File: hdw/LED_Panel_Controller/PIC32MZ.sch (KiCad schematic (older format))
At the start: 3 parts

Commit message: more schematic development
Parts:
- removed U?: PIC32MZ2048EFG100-250_IPF, Housings_QFP:TQFP-100_14x14mm_Pitch0.5mm, symbol Custom_Library:PIC32MZ2048EFG100_IPF
- added U?: PIC32MZ2048EFG100_IPF, Housings_QFP:TQFP-100_14x14mm_Pitch0.5mm, symbol Custom_Library:PIC32MZ2048EFG100_IPF
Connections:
- net +3.3VA_MZ: now also U?.30 (AVDD)
- net +3V3: now also U?.14 (VDD), U?.37 (VDD), U?.46 (VDD), U?.62 (VDD), U?.74 (VDD), U?.83 (VDD), U?.93 (VDD)
- net B0_POS3P3: now also U?.100 (RE4/EBID4/AN18/PMD4)
- net B1_POS3P3: now also U?.3 (RE5/EBID5/AN17/RPE5/PMD5)
- net CPU_Trap_LED: now also U?.71 (RD0/EMDIO/AEMDIO/RPD0/RTCC/INT0)
- net Cap_Touch_Mode: now also U?.11 (RG7/EBIA4/AN13/C1INC/ECRS/RPG7/SDA4/PMA4)
- net Cap_Touch_Power: now also U?.10 (RG6/AN14/C1IND/ECOL/RPG6/SCK2)
- net Error_LED: now also U?.66 (RA14/AETXCLK/RPA14/SCL1)
- net FLASH_SPI_MISO: now also U?.33 (RB9/EBIA7/AN49/RPB9/PMA7)
- net FLASH_SPI_MOSI: now also U?.34 (RB10/EBIA13/CVREFOUT/AN5/RPB10/PMA13)
- net FLASH_SPI_SCK: now also U?.43 (RB14/EBIA1/AN9/ERXD2/AETXD3/RPB14/SCK3/PMA1)
- net Flash_Slideshow_Mode_LED: now also U?.87 (RG1/EBID9/ETXERR/RPG1/PMD9)
- net G0_POS3P3: now also U?.98 (RE2/EBID2/PMD2)
- net G1_POS3P3: now also U?.99 (RE3/EBID3/RPE3/PMD3)
- net GND: now also U?.13 (VSS), U?.36 (VSS), U?.45 (VSS), U?.52 (VBUS3V3), U?.53 (VSS), U?.63 (VSS), U?.75 (VSS), U?.84 (VSS), U?.92 (VSS)
- net GNDA_MZ: now also U?.31 (AVSS)
- net Heartbeat_LED: now also U?.68 (RD9/EBIA15/RPD9/PMCS2/PMA15)
- net I2C_SCL: now also U?.65 (RF5/EBIA8/RPF5/SCL5/PMA8)
- net I2C_SDA: now also U?.64 (RF4/EBIA9/RPF4/SDA5/PMA9)
- net PGOOD_LED_SHDN: now also U?.58 (RF8/EBIRDY2/RPF8/SCL3)
- net PIC32MZ_ICSPCLK: now also U?.26 (RB6/PGEC2/AN46/RPB6)
- net PIC32MZ_ICSPDAT: now also U?.27 (RB7/PGED2/AN47/RPB7)
- net PIC32MZ_POSC_EC: now also U?.49 (RC12/OSC1/CLKI)
- net PIC32MZ_REFCLK1: now also U?.72 (RC13/SOSCI/RPC13)
- net PIC32MZ_SOSC: now also U?.73 (RC14/SOSCO/RPC14/T1CK)
- net PIC32MZ_UART_RX: now also U?.77 (RD2/EBID14/ETXEN/RPD2/PMD14)
- net PIC32MZ_UART_TX: now also U?.78 (RD3/EBID15/ETXCLK/RPD3/PMD15)
- net POS12_PGOOD: now also U?.35 (RB11/AN6/ERXERR/AETXERR)
- net POS3P3_PGOOD: now also U?.40 (RF12/TDO/EBIA17/AN31/RPF12)
- net POS5_PGOOD: now also U?.41 (RB12/EBIA11/AN7/ERXD0/AECRS/PMA11)
- net POS5_RUN: now also U?.42 (RB13/AN8/ERXD1/AECOL)
- net POS5_USB_PGOOD: now also U?.57 (RF2/EBIRDY3/RPF2/SDA3)
- net Panel_CLK_POS3P3: now also U?.8 (RC3/~EBIWE~/AN20/RPC3/PMWR)
- net Panel_Dim_PWM: now also U?.12 (RG8/EBIA3/AN12/C2IND/ERXDV/ECRSDV/AERXDV/AECRSDV/RPG8/SCL4/PMA3)
- net Panel_LAT_POS3P3: now also U?.20 (RB5/AN45/C1INA/RPB5)
- net Prog1_Mode_LED: now also U?.16 (RG9/EBIA2/AN11/C2INC/ERXCLK/EREFCLK/AERXCLK/AEREFCLK/RPG9/PMA2)
- net Prog2_Mode_LED: now also U?.96 (RG12/TRD1/SQID1)
- net Prog3_Mode_LED: now also U?.97 (RG13/TRD0/SQID0)
- net Prog4_Mode_LED: now also U?.95 (RG14/TRD2/SQID2)
- net Prog5_Mode_LED: now also U?.1 (RG15/AN23/AERXERR)
- net R0_POS3P3: now also U?.91 (RE0/EBID0/PMD0)
- net R1_POS3P3: now also U?.94 (RE1/EBID1/PMD1)
- net Reset_LED: now also U?.67 (RA15/AETXEN/RPA15/SDA1)
- net Row_A_POS3P3: now also U?.25 (RB0/PGED1/AN0/RPB0)
- net Row_B_POS3P3: now also U?.24 (RB1/PGEC1/AN1/RPB1)
- net Row_C_POS3P3: now also U?.23 (RB2/AN2/C2INB/RPB2)
- net Row_D_POS3P3: now also U?.22 (RB3/AN3/C2INA/RPB3)
- net Row_E_POS3P3: now also U?.21 (RB4/AN4/C1INB)
- net SD_SPI_MISO: now also U?.6 (RC1/EBIA6/AN22/RPC1/PMA6)
- net SD_SPI_MOSI: now also U?.86 (RF1/EBID10/ETXD0/RPF1/PMD10)
- net SD_SPI_SCK: now also U?.39 (RF13/TDI/EBIA18/AN30/RPF13/SCK5)
- net USB_Stream_Mode_LED: now also U?.88 (RG0/EBID8/RPG0/PMD8)
- net VBAT_ADC: now also U?.18 (RE8/AN25/AERXD0/RPE8)
- net VBAT_PGOOD: now also U?.44 (RB15/EBIA0/AN10/ERXD3/AETXD2/RPB15/OCFB/PMA0)
- net WIFI_CHIP_EN: now also U?.79 (RD12/EBID12/ETXD2/RPD12/PMD12)
- net WIFI_SPI_MISO: now also U?.48 (RD15/AN33/AETXD1/RPD15/SCK6)
- net WIFI_SPI_MOSI: now also U?.70 (RD11/EMDC/AEMDC/RPD11)
- net WIFI_SPI_SCK: now also U?.69 (RD10/RPD10/SCK4)
- net WIFI_Stream_Mode_LED: now also U?.32 (RB8/EBIA10/AN48/RPB8/PMA10)
- net WIFI_WAKE: now also U?.82 (RD5/~SQICS1~/RPD5)
- net ~FLASH_SPI_CE0: now also U?.17 (RA0/TMS/EBIA16/AN24)
- net ~FLASH_SPI_CE1: now also U?.38 (RA1/TCK/EBIA19/AN29)
- net ~FLASH_SPI_CE2: now also U?.59 (RA2/~EBICS0~/SCL2)
- net ~FLASH_SPI_CE3: now also U?.60 (RA3/EBIRDY1/SDA2)
- net ~FLASH_SPI_CE4: now also U?.61 (RA4/EBIA14/PMCS1/PMA14)
- net ~FLASH_SPI_CE5: now also U?.2 (RA5/EBIA5/AN34/PMA5)
- net ~FLASH_SPI_CE6: now also U?.89 (RA6/TRCLK/SQICLK)
- net ~FLASH_SPI_CE7: now also U?.90 (RA7/TRD3/SQID3)
- net ~PIC32MZ_MCLR: now also U?.15 (~MCLR~)
- net ~Panel_OE_POS3P3: now also U?.76 (RD1/RPD1/SCK1)
- net ~SD_CARD_DET: now also U?.9 (RC4/~EBIOE~/AN19/RPC4/PMRD)
- net ~SD_SPI_CS: now also U?.7 (RC2/EBIA12/AN21/RPC2/PMA12)
- net ~WIFI_IRQN: now also U?.47 (RD14/AN32/AETXD0/RPD14)
- net ~WIFI_RESET: now also U?.81 (RD4/~SQICS0~/RPD4)
- net ~WIFI_SPI_SS: now also U?.80 (RD13/EBID13/ETXD3/PMD13)
- new net Void_Mode_LED: U?.19 (RE9/AN26/AERXD1/RPE9)
- no-connect marks 5 -> 9
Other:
- moved on the sheet: R?

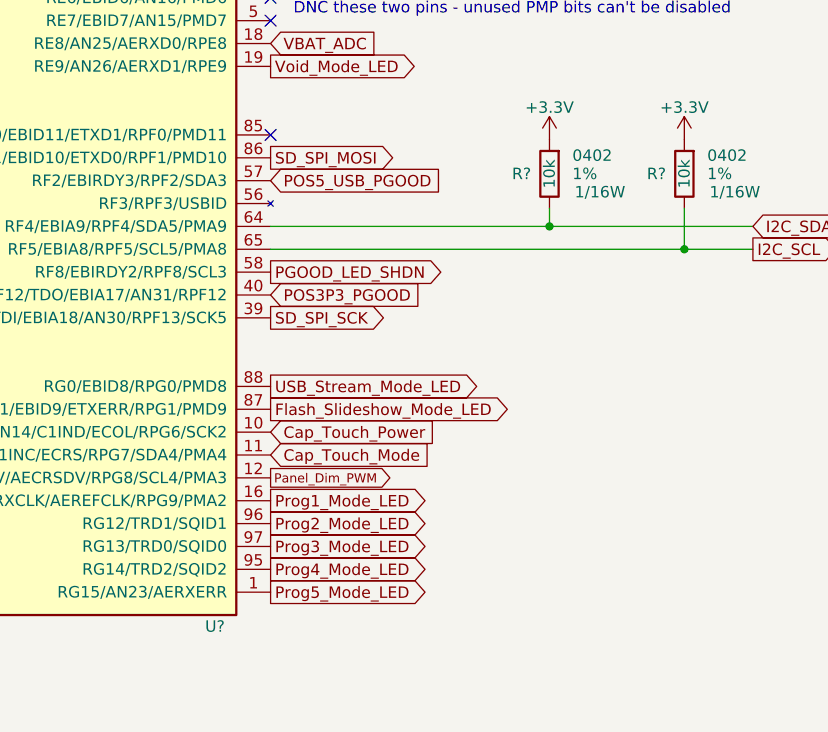
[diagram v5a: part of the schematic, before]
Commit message: assigned I2C addresses
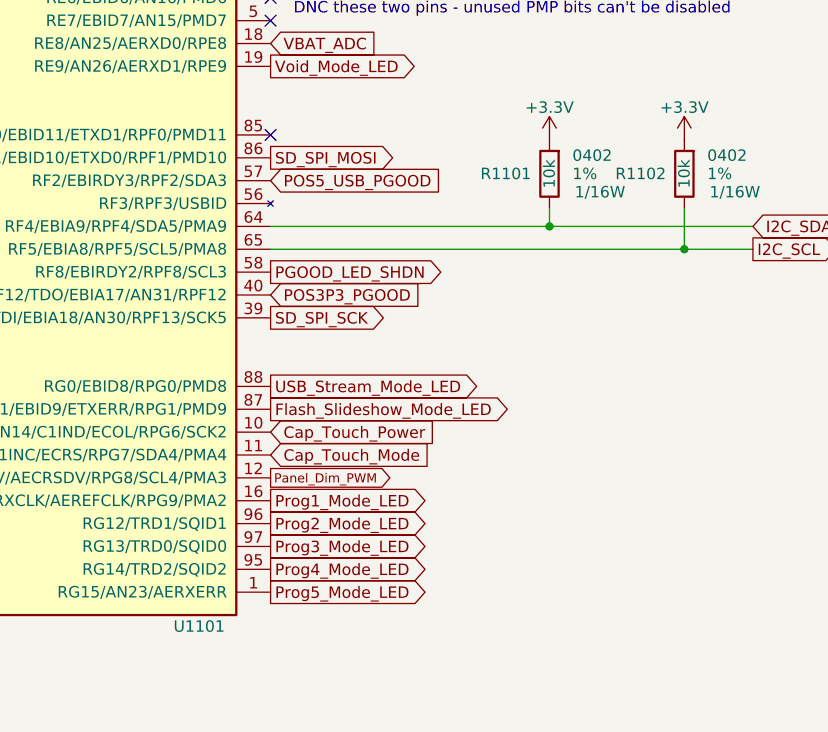
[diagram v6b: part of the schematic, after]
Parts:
- gave numbers to parts that had none: 3
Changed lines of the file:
@@
 ~PIC32MZ_MCLR
 $Comp
-L power:GND #PWR?
+L power:GND #PWR01101
 U 1 1 5CB14B21
 P 2910 5580
-F 0 "#PWR?" H 2910 5330 50  0001 C CNN
+F 0 "#PWR01101" H 2910 5330 50  0001 C CNN
 F 1 "GND" H 2910 5430 50  0000 C CNN
 F 2 "" H 2910 5580 50  0001 C CNN
@@
 AR Path="/5EAE4A89/5EB7DAD1" Ref="R?"  Part="1"
 AR Path="/5EAE2F23/5EB7DAD1" Ref="R?"  Part="1"
-AR Path="/5F5829D3/5EB7DAD1" Ref="R?"  Part="1"
-F 0 "R?" H 8750 4170 50  0000 R CNN
+AR Path="/5F5829D3/5EB7DAD1" Ref="R1102"  Part="1"
+F 0 "R1102" H 8750 4170 50  0000 R CNN
 F 1 "10k" V 8830 4170 50  0000 C CNN
 F 2 "Resistors_SMD:R_0402" H 8830 4170 50  0001 C CNN
@@
 $EndComp
 $Comp
-L power:+3.3V #PWR?
+L power:+3.3V #PWR01107
 U 1 1 5EB7DAD7
 P 8830 4020
-F 0 "#PWR?" H 8830 3870 50  0001 C CNN
+F 0 "#PWR01107" H 8830 3870 50  0001 C CNN
 F 1 "+3.3V" H 8830 4160 50  0000 C CNN
 F 2 "" H 8830 4020 50  0001 C CNN
@@
 AR Path="/5EAE4A89/5EB7DEAB" Ref="R?"  Part="1"
 AR Path="/5EAE2F23/5EB7DEAB" Ref="R?"  Part="1"
-AR Path="/5F5829D3/5EB7DEAB" Ref="R?"  Part="1"
-F 0 "R?" H 8160 4170 50  0000 R CNN
+AR Path="/5F5829D3/5EB7DEAB" Ref="R1101"  Part="1"
+F 0 "R1101" H 8160 4170 50  0000 R CNN
 F 1 "10k" V 8240 4170 50  0000 C CNN
 F 2 "Resistors_SMD:R_0402" H 8240 4170 50  0001 C CNN
@@
 $EndComp
 $Comp
-L power:+3.3V #PWR?
+L power:+3.3V #PWR01106
 U 1 1 5EB7DEB5
 P 8240 4020
-F 0 "#PWR?" H 8240 3870 50  0001 C CNN
+F 0 "#PWR01106" H 8240 3870 50  0001 C CNN
 F 1 "+3.3V" H 8240 4160 50  0000 C CNN
 F 2 "" H 8240 4020 50  0001 C CNN
@@
 ~WIFI_IRQN
 $Comp
-L Custom_Library:GNDA_MZ #PWR?
+L Custom_Library:GNDA_MZ #PWR01103
 U 1 1 5FFB96A6
 P 4370 6330
-F 0 "#PWR?" H 4370 6080 50  0001 C CNN
+F 0 "#PWR01103" H 4370 6080 50  0001 C CNN
 F 1 "GNDA_MZ" H 4370 6180 50  0000 C CNN
 F 2 "" H 4370 6330 50  0001 C CNN
@@
 	4370 6330 4370 6250
 $Comp
-L Custom_Library:+3.3VA_MZ #PWR?
+L Custom_Library:+3.3VA_MZ #PWR01102
 U 1 1 5FFB9C17
 P 4370 970
-F 0 "#PWR?" H 4370 820 50  0001 C CNN
+F 0 "#PWR01102" H 4370 820 50  0001 C CNN
 F 1 "+3.3VA_MZ" H 4370 1110 50  0000 C CNN
 F 2 "" H 4370 970 50  0001 C CNN
@@
 	5070 1010 4970 1010
 $Comp
-L power:+3.3V #PWR?
+L power:+3.3V #PWR01104
 U 1 1 5FFBDFF7
 P 4870 970
-F 0 "#PWR?" H 4870 820 50  0001 C CNN
+F 0 "#PWR01104" H 4870 820 50  0001 C CNN
 F 1 "+3.3V" H 4870 1110 50  0000 C CNN
 F 2 "" H 4870 970 50  0001 C CNN
@@
 	5020 6290 4970 6290
 $Comp
-L power:GND #PWR?
+L power:GND #PWR01105
 U 1 1 5FFC1E1C
 P 5020 6330
-F 0 "#PWR?" H 5020 6080 50  0001 C CNN
+F 0 "#PWR01105" H 5020 6080 50  0001 C CNN
 F 1 "GND" H 5020 6180 50  0000 C CNN
 F 2 "" H 5020 6330 50  0001 C CNN
@@
 ~Panel_OE_POS3P3
 $Comp
-L Custom_Library:PIC32MZ2048EFG100_IPF U?
+L Custom_Library:PIC32MZ2048EFG100_IPF U1101
 U 1 1 605C2FEE
 P 5020 3650
-F 0 "U?" H 6820 1150 50  0000 R CNN
+F 0 "U1101" H 6820 1150 50  0000 R CNN
 F 1 "PIC32MZ2048EFG100_IPF" H 5020 4250 50  0000 C CNN
 F 2 "Housings_QFP:TQFP-100_14x14mm_Pitch0.5mm" H 5020 3650 50  0001 C CNN

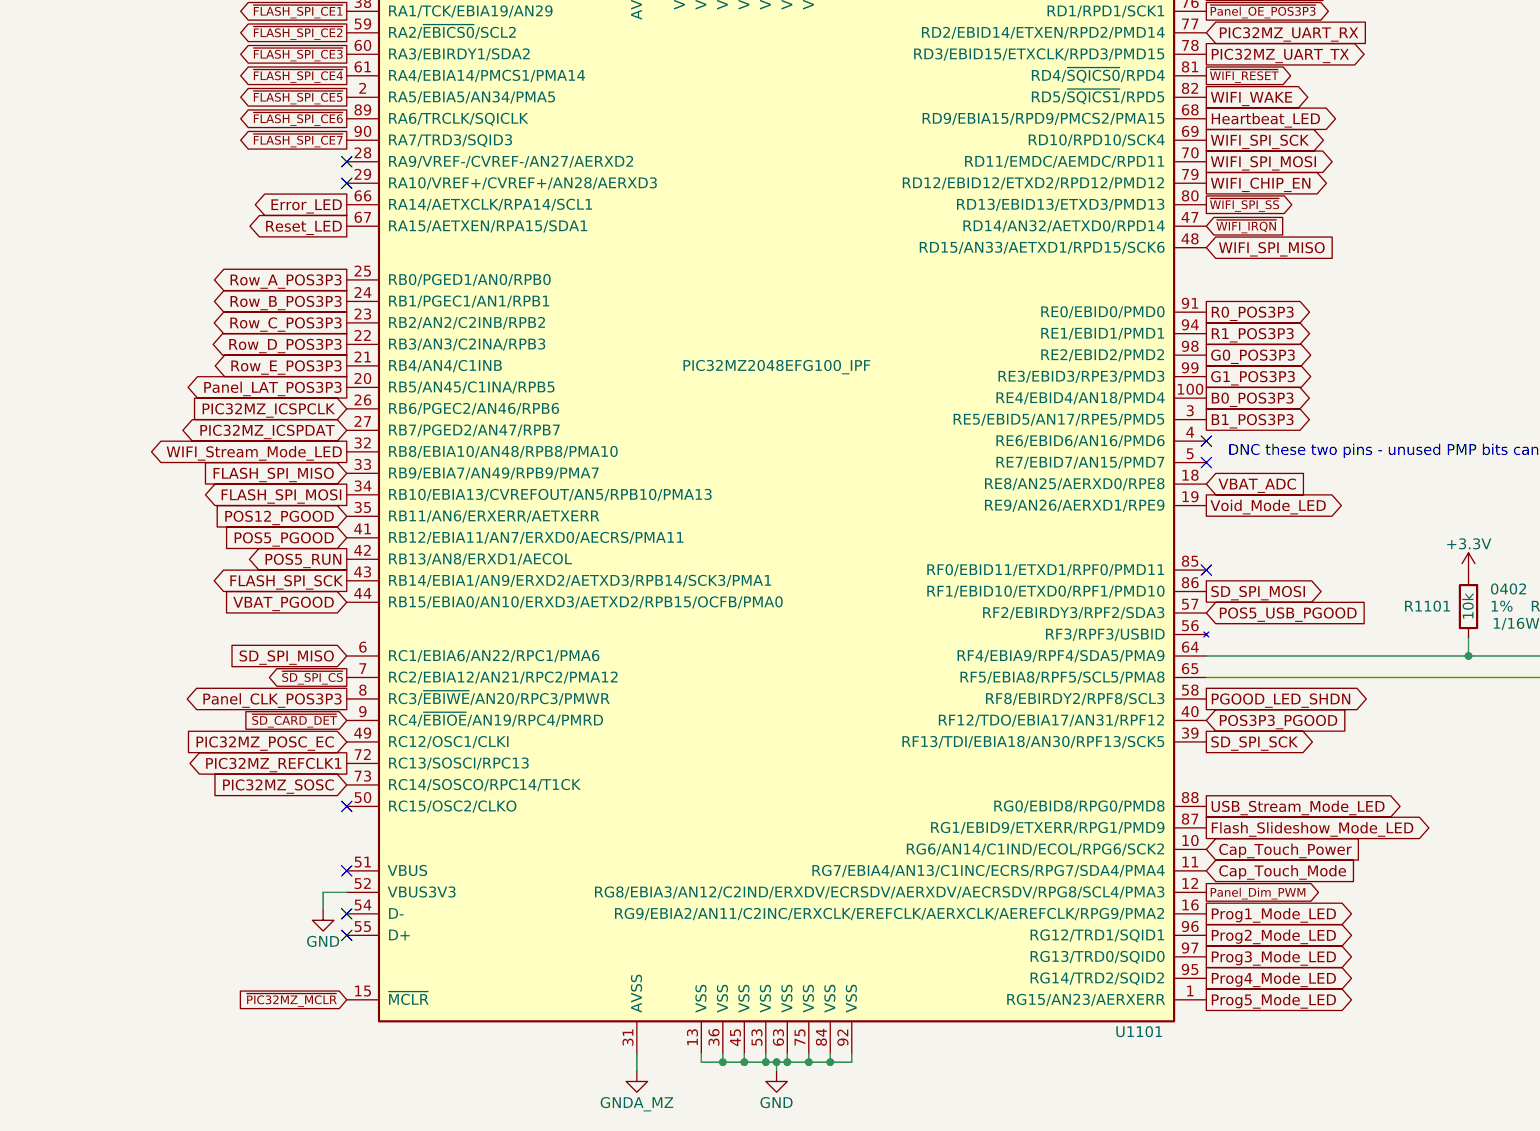
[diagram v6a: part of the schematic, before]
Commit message: ran erc, annotated schematic, added hardstraps to MCU
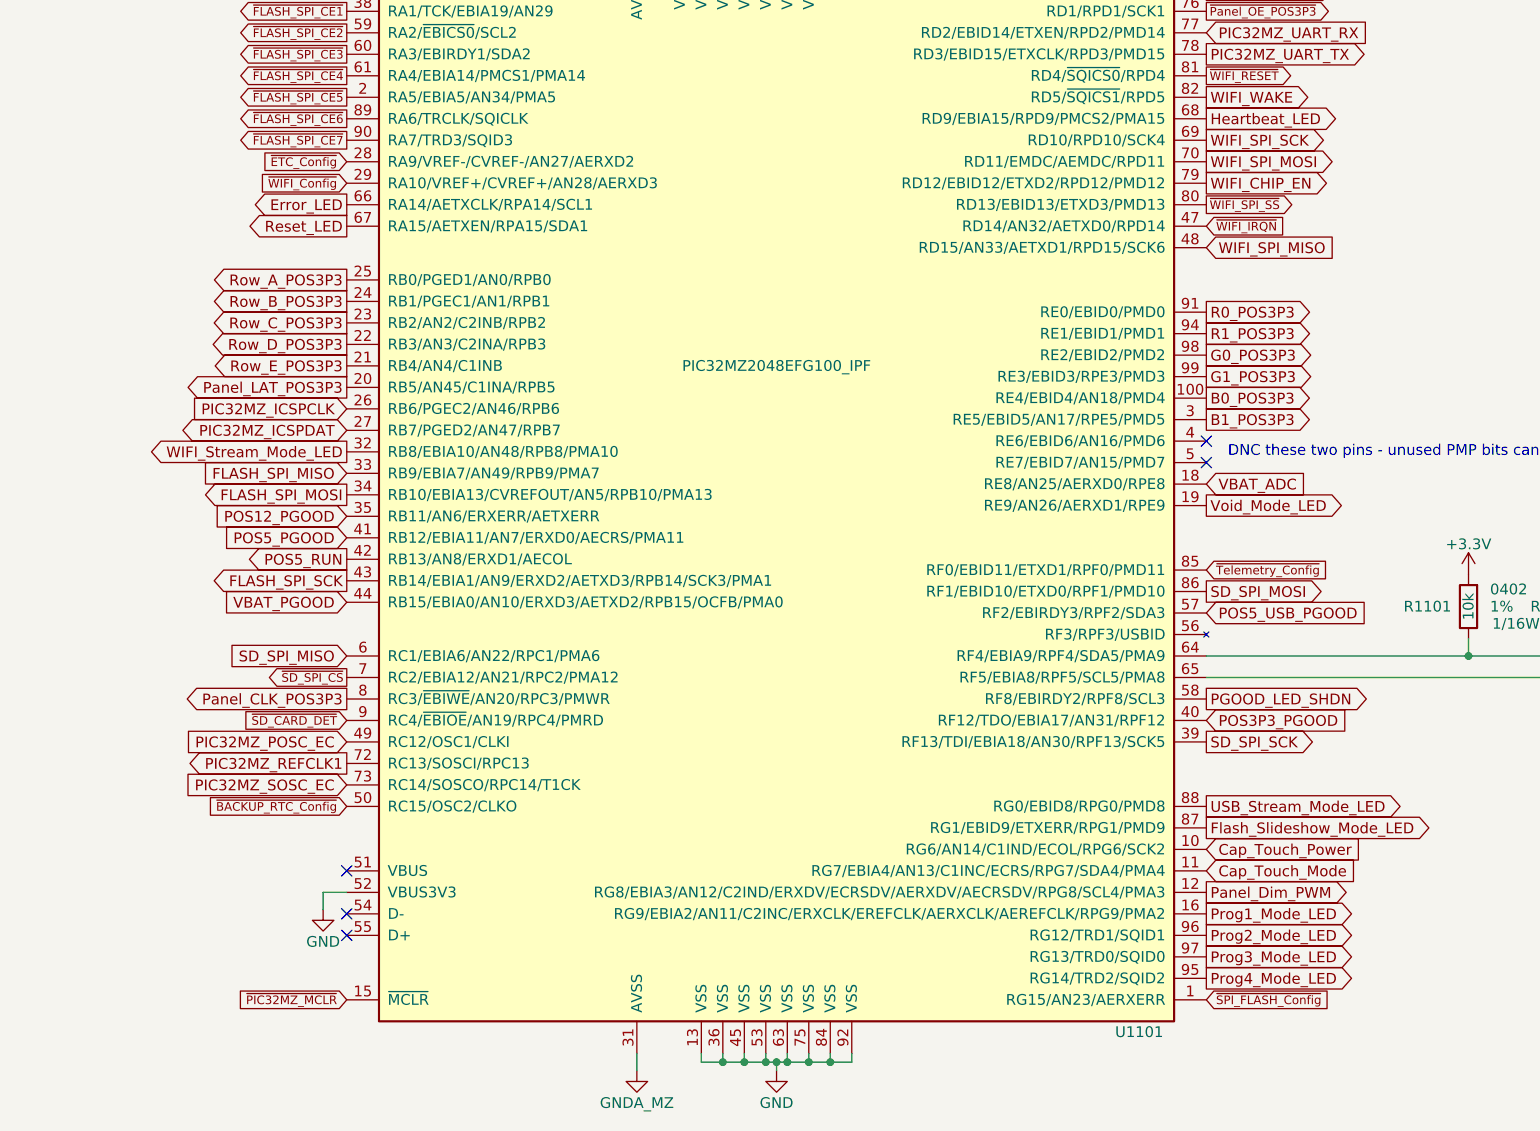
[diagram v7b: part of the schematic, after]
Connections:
- net ~ETC_Config: now reaches U1101.28 (RA9/VREF-/CVREF-/AN27/AERXD2)
- net ~WIFI_Config: now reaches U1101.29 (RA10/VREF+/CVREF+/AN28/AERXD3)
- net ~BACKUP_RTC_Config: now reaches U1101.50 (RC15/OSC2/CLKO)
- net ~Telemetry_Config: now reaches U1101.85 (RF0/EBID11/ETXD1/RPF0/PMD11)
- net PIC32MZ_SOSC renamed PIC32MZ_SOSC_EC
- net Prog5_Mode_LED renamed ~SPI_FLASH_Config
- no-connect marks 9 -> 5
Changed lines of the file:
@@
 PIC32MZ_POSC_EC
 Text GLabel 3020 5000 0    50   Input ~ 0
-PIC32MZ_SOSC
+PIC32MZ_SOSC_EC
 Text GLabel 7020 1700 2    40   Output ~ 0
 ~WIFI_RESET
@@
 Text GLabel 3020 3150 0    50   Output ~ 0
 Panel_LAT_POS3P3
-Text GLabel 7020 5500 2    40   Output ~ 0
+Text GLabel 7020 5500 2    50   Output ~ 0
 Panel_Dim_PWM
 Text GLabel 3020 4600 0    50   Output ~ 0
@@
 Text GLabel 7020 5700 2    50   Output ~ 0
 Prog2_Mode_LED
-Text GLabel 7020 6000 2    50   Output ~ 0
-Prog5_Mode_LED
 Text GLabel 7020 5800 2    50   Output ~ 0
 Prog3_Mode_LED
@@
 	1    0    0    -1
 $EndComp
-NoConn ~ 3020 5100
-NoConn ~ 3020 2100
-NoConn ~ 3020 2200
-NoConn ~ 7020 4000
+Text GLabel 7020 4000 2    40   Input ~ 0
+~Telemetry_Config
+Text GLabel 3020 2100 0    40   Input ~ 0
+~ETC_Config
+Text GLabel 3020 2200 0    40   Input ~ 0
+~WIFI_Config
+Text GLabel 3020 5100 0    40   Input ~ 0
+~BACKUP_RTC_Config
+Text GLabel 7020 6000 2    40   Input ~ 0
+~SPI_FLASH_Config
 $EndSCHEMATC
